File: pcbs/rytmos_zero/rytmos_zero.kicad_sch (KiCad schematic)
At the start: 14 parts, among them J1 DAC, J2 Conn_01x02_Pin, U1 Pico, U2 LM7805_TO220

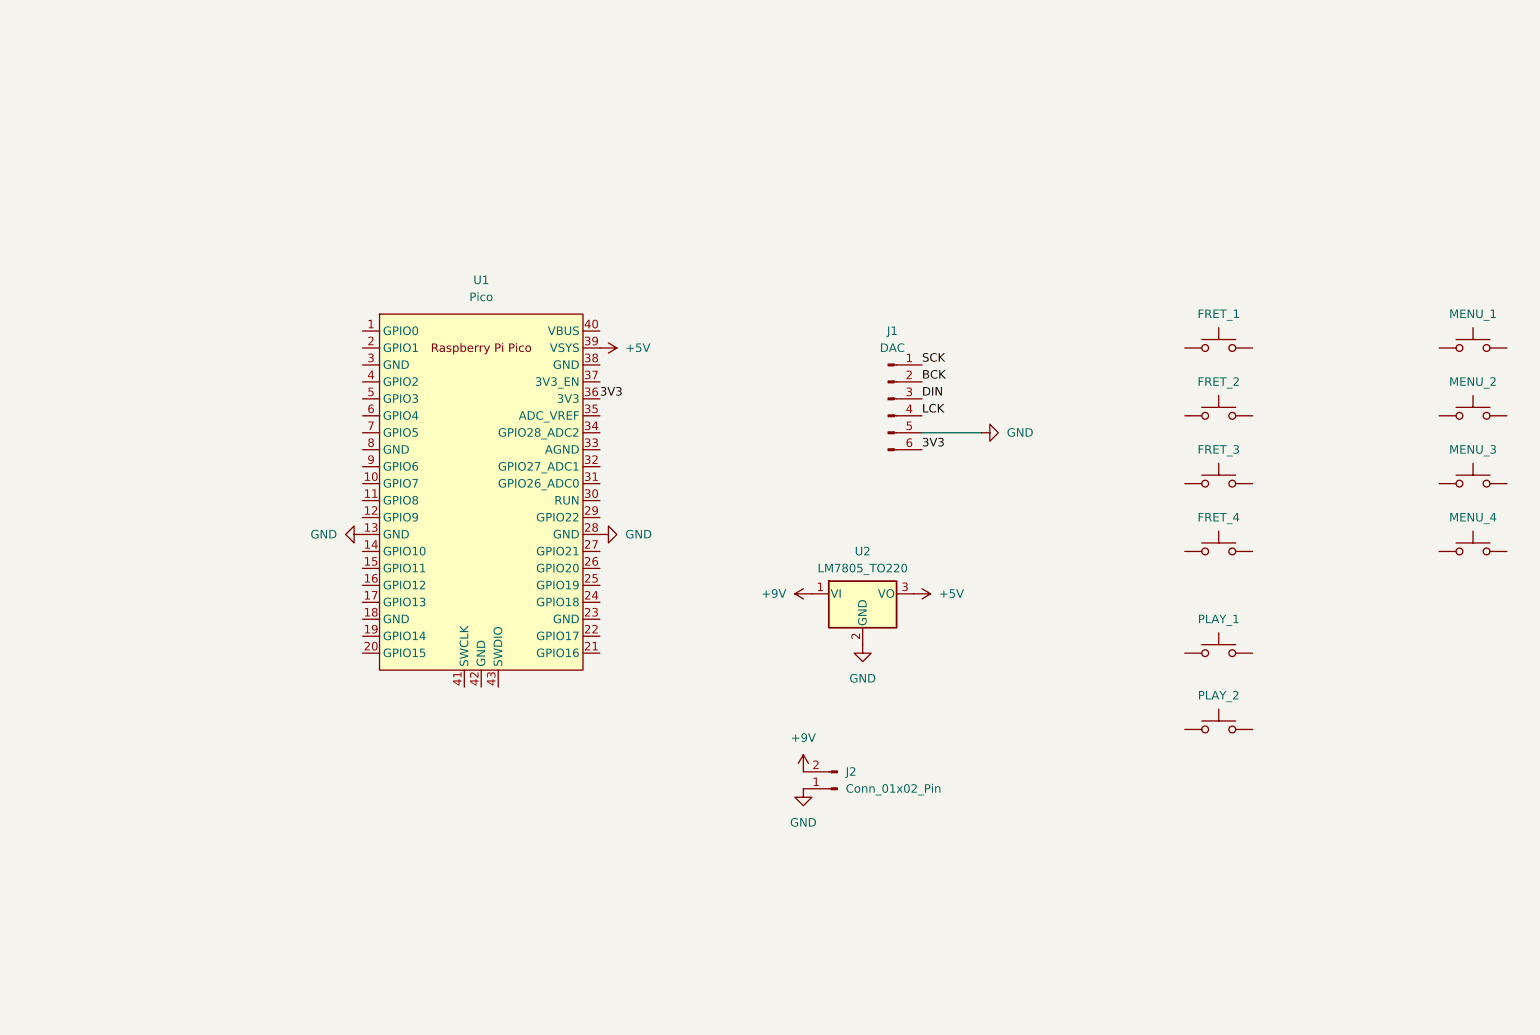
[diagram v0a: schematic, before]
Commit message: Pico Piano PCB changes
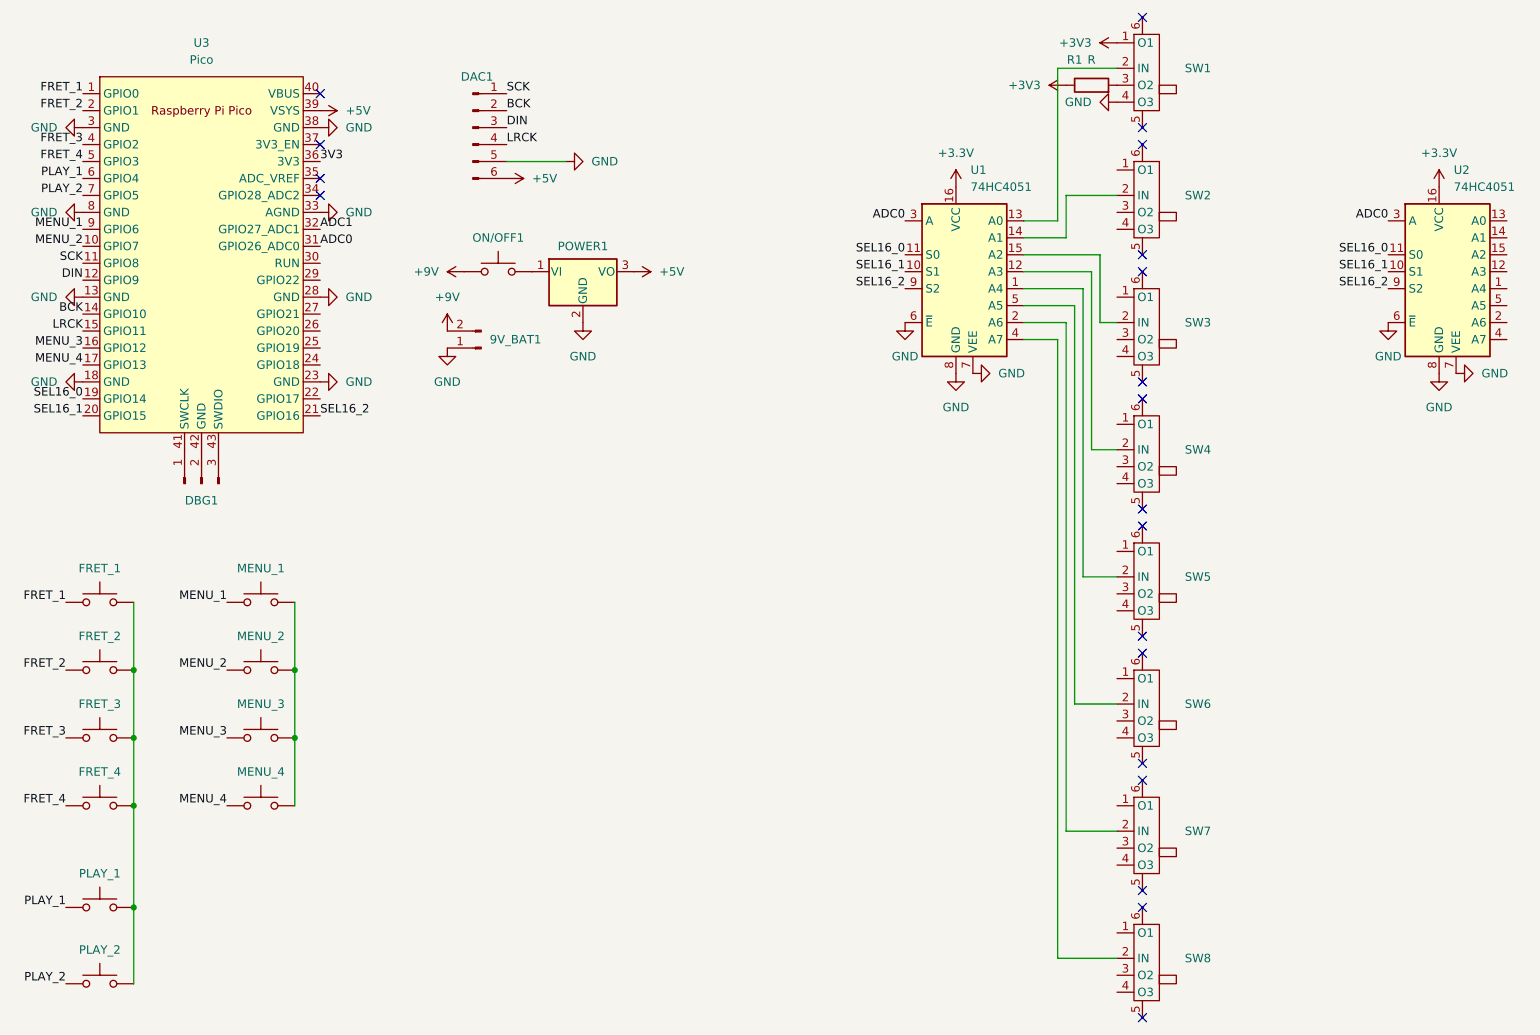
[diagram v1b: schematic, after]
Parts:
- removed J1: DAC, symbol Connector:Conn_01x06_Pin
- removed J2: Conn_01x02_Pin, symbol Connector:Conn_01x02_Pin
- removed U1: Pico, RPi_Pico:RPi_Pico_SMD_TH, symbol pico:Pico
- removed U2: LM7805_TO220, Package_TO_SOT_THT:TO-220-3_Vertical, symbol Regulator_Linear:LM7805_TO220
- added 9V_BAT1: Conn_01x02_Pin, Connector_PinSocket_2.54mm:PinSocket_1x02_P2.54mm_Vertical, symbol Connector:Conn_01x02_Pin
- added DAC1: DAC, rytmos:PCM5102_BREAKOUT, symbol Connector:Conn_01x06_Pin
- added DBG1: Conn_01x03_Pin, Connector_PinSocket_2.54mm:PinSocket_1x03_P2.54mm_Vertical, symbol Connector:Conn_01x03_Pin
- added ON/OFF1: SW_Push, Connector_PinHeader_2.54mm:PinHeader_1x03_P2.54mm_Vertical, symbol Switch:SW_Push
- added POWER1: LM7805_TO220, Package_TO_SOT_THT:TO-220-3_Vertical, symbol Regulator_Linear:LM7805_TO220
- added R1: R, symbol Device:R
- added SW1, SW2, SW3, SW4, SW5, SW6, SW7, SW8: ~, symbol rytmos:SS13D07VG4
- added U1, U2: 74HC4051, symbol 74xx:74HC4051
- added U3: Pico, MCU_RaspberryPi_and_Boards:RPi_Pico_SMD_TH, symbol pico:Pico
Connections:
- net +5V: now also DAC1.6 (Pin_6), POWER1.3 (VO), U3.39 (VSYS)
- net +9V: now also 9V_BAT1.2 (Pin_2), ON/OFF1.1
- net 3V3: now also U3.36 (3V3)
- net BCK: now also DAC1.2 (Pin_2), U3.14 (GPIO10)
- net DIN: now also DAC1.3 (Pin_3), U3.12 (GPIO9)
- net GND: now also 9V_BAT1.1 (Pin_1), DAC1.5 (Pin_5), POWER1.2 (GND), SW1.4 (O3), U1.6 (~{E}), U1.7 (VEE), U1.8 (GND), U2.6 (~{E}), U2.7 (VEE), U2.8 (GND), U3.13 (GND), U3.18 (GND), U3.23 (GND), U3.28 (GND), U3.3 (GND), U3.33 (AGND), U3.38 (GND), U3.8 (GND)
- net SCK: now also DAC1.1 (Pin_1), U3.11 (GPIO8)
- net PLAY_1: now reaches PLAY_1.1
- net PLAY_1: now also U3.6 (GPIO4)
- net at PLAY_1.2: now also FRET_1.2, FRET_2.2, FRET_3.2, FRET_4.2, PLAY_2.2
- net FRET_2: now reaches FRET_2.1
- net FRET_2: now also U3.2 (GPIO1)
- net MENU_2: now reaches MENU_2.1
- net MENU_2: now also U3.10 (GPIO7)
- net at MENU_2.2: now also MENU_1.2, MENU_3.2, MENU_4.2
- net MENU_3: now reaches MENU_3.1
- net MENU_3: now also U3.16 (GPIO12)
- net FRET_1: now reaches FRET_1.1
- net FRET_1: now also U3.1 (GPIO0)
- net FRET_4: now reaches FRET_4.1
- net FRET_4: now also U3.5 (GPIO3)
- net MENU_4: now reaches MENU_4.1
- net MENU_4: now also U3.17 (GPIO13)
- net PLAY_2: now reaches PLAY_2.1
- net PLAY_2: now also U3.7 (GPIO5)
- net FRET_3: now reaches FRET_3.1
- net FRET_3: now also U3.4 (GPIO2)
- net MENU_1: now reaches MENU_1.1
- net MENU_1: now also U3.9 (GPIO6)
- new net: ON/OFF1.2, POWER1.1 (VI)
- new net: SW2.2 (IN), U1.14 (A1)
- new net: SW4.2 (IN), U1.12 (A3)
- new net: SW3.2 (IN), U1.15 (A2)
- new net: SW7.2 (IN), U1.2 (A6)
- new net: DBG1.1 (Pin_1), U3.41 (SWCLK)
- new net: DBG1.2 (Pin_2), U3.42 (GND)
- new net: DBG1.3 (Pin_3), U3.43 (SWDIO)
- new net: SW1.2 (IN), U1.13 (A0)
- new net: R1.2, SW1.3 (O2)
- new net: SW5.2 (IN), U1.1 (A4)
- new net: SW8.2 (IN), U1.4 (A7)
- new net: SW6.2 (IN), U1.5 (A5)
- new net +3.3V: U1.16 (VCC), U2.16 (VCC)
- new net +3V3: R1.1, SW1.1 (O1)
- new net ADC0: U1.3 (A), U2.3 (A), U3.31 (GPIO26_ADC0)
- new net ADC1: U3.32 (GPIO27_ADC1)
- new net LRCK: DAC1.4 (Pin_4), U3.15 (GPIO11)
- new net SEL16_0: U1.11 (S0), U2.11 (S0), U3.19 (GPIO14)
- new net SEL16_1: U1.10 (S1), U2.10 (S1), U3.20 (GPIO15)
- new net SEL16_2: U1.9 (S2), U2.9 (S2), U3.21 (GPIO16)
- no-connect marks 0 -> 20
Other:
- moved on the sheet: FRET_1, FRET_2, FRET_3, FRET_4, MENU_1, MENU_2, MENU_3, MENU_4, PLAY_1, PLAY_2

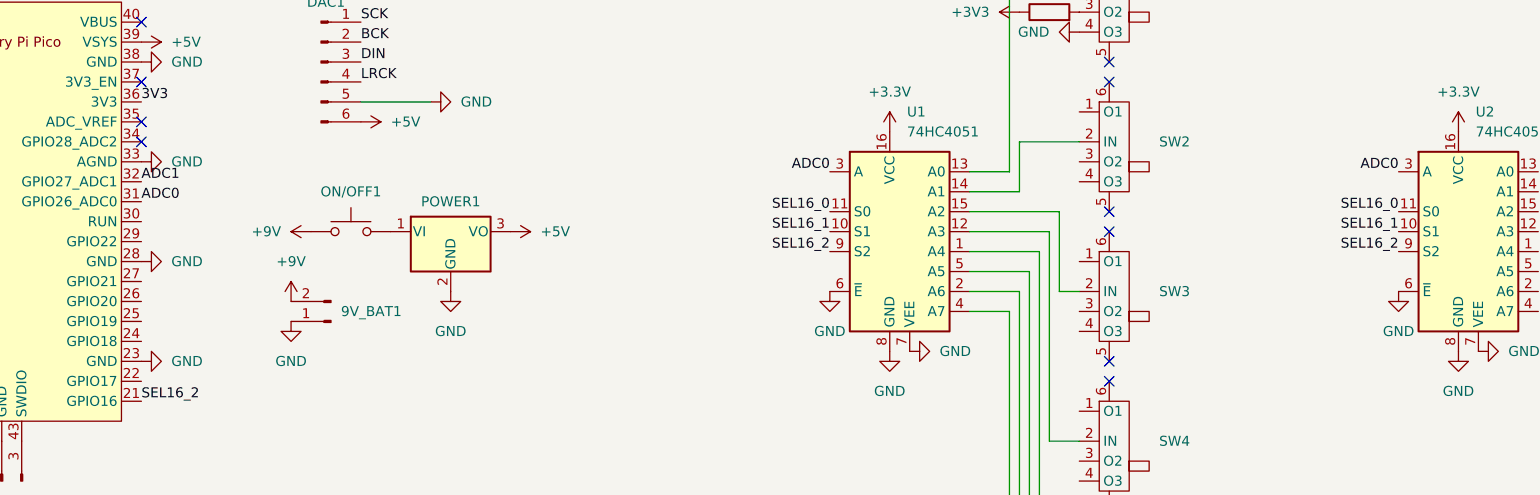
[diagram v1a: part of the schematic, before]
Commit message: Add drum synth
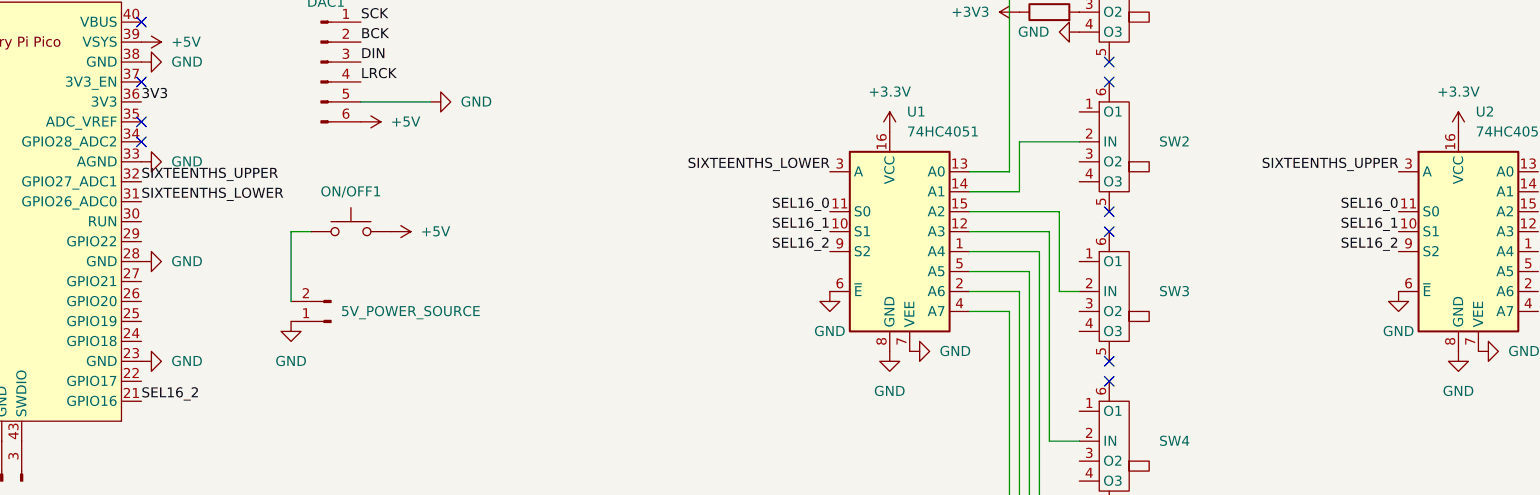
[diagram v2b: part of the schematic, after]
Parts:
- removed POWER1: LM7805_TO220, Package_TO_SOT_THT:TO-220-3_Vertical, symbol Regulator_Linear:LM7805_TO220
- renumbered 9V_BAT1 to 5V_POWER_SOURCE
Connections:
- net +5V: now also ON/OFF1.2
- net +9V: no longer names the net of 5V_POWER_SOURCE.2 (Pin_2), ON/OFF1.1
- net ADC0 renamed SIXTEENTHS_LOWER
- net SIXTEENTHS_LOWER: no longer U2.3 (A)
- net ADC1 renamed SIXTEENTHS_UPPER
- net SIXTEENTHS_UPPER: now also U2.3 (A)
